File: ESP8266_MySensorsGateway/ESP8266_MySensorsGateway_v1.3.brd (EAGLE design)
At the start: 50 x 24.9 mm, 38 parts, among them IC1 3V3

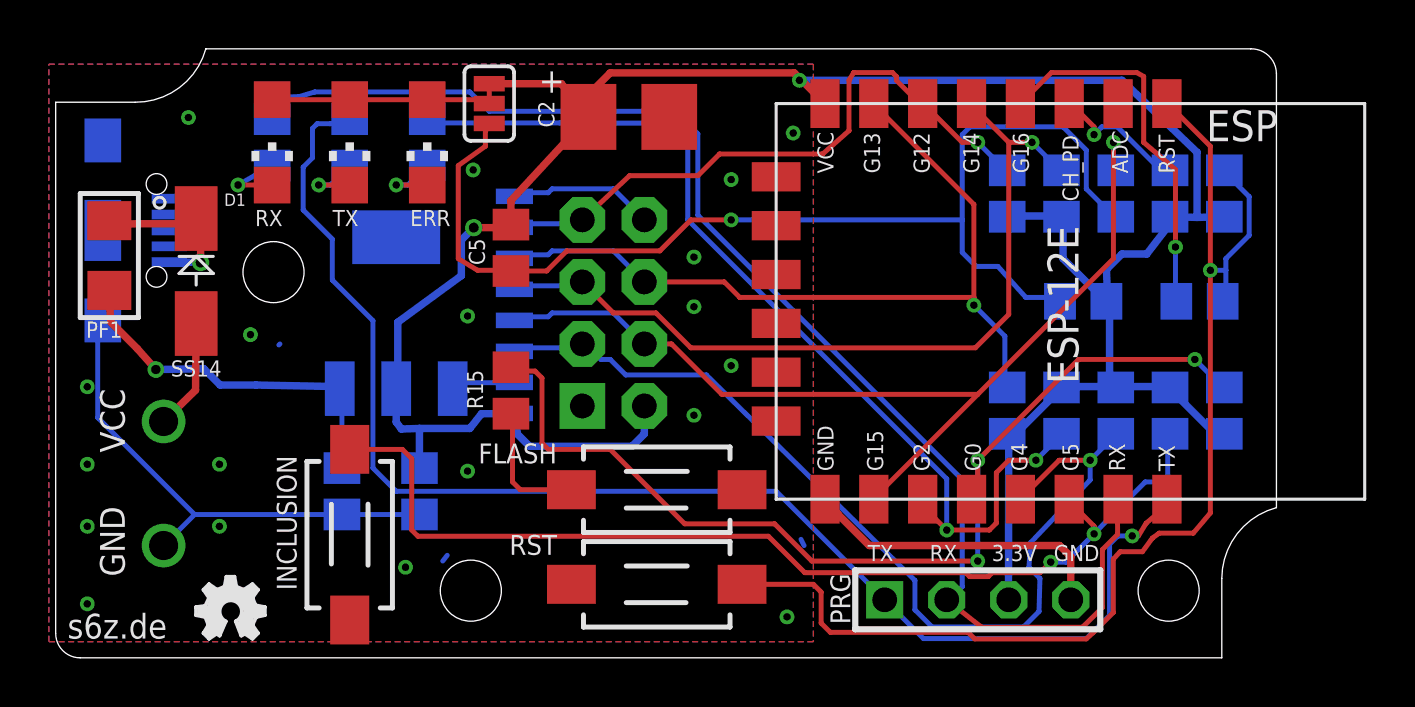
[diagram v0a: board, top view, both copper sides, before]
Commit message: fix (Radio GND), v.1.3.2
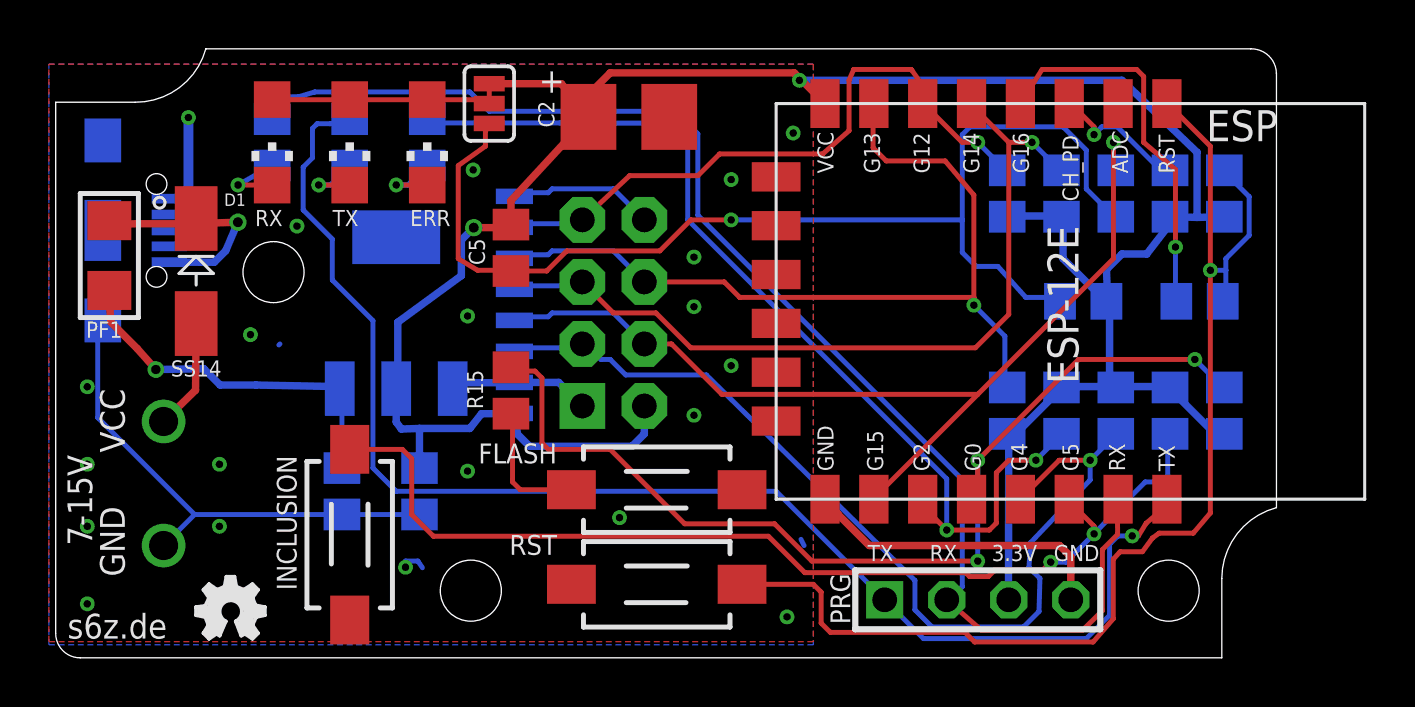
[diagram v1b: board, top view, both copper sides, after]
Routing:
- net GND: track 84.0 -> 93.4 mm, vias 20 -> 22
- net VUSB: track 7.08 -> 10.7 mm
- net MOSI: track 33.7 -> 35.1 mm
- net MISO: track 25.8 -> 26.4 mm
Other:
- board text added: "ESP/MS-GW/v1.3.2/22.05.2016"
- board text removed: "ESP/MS-GW/v1.3.1/23.03.2016"
